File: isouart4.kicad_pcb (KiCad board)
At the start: 2 copper layers, 89 x 99 mm, 78 parts, among them J1 USB_B, J2 Conn_01x04, J3 Conn_01x04, J4 Conn_01x04, J5 Conn_01x04, U1 CH344Q, U10 74HC123, U11 74HC123, U12 74HC123, U13 74HC123, U2 π122U31, U3 AMS1117-3.3, U4 π122U31, U5 π122U31, U6 π122U31, X1 ASV-xxxMHz

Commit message: pcb-route all uart channels
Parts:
- removed C4: 100n, Capacitor_SMD:C_0805_2012Metric_Pad1.18x1.45mm_HandSolder
- removed C6: 12p, Capacitor_SMD:C_0805_2012Metric_Pad1.18x1.45mm_HandSolder
- removed L3: L_Ferrite_Small, Inductor_SMD:L_TDK_NLV25_2.5x2.0mm
- removed X1: ASV-xxxMHz, Oscillator:Oscillator_SMD_Abracon_ASV-4Pin_7.0x5.1mm
- added C10: 100n, Capacitor_SMD:C_0805_2012Metric_Pad1.18x1.45mm_HandSolder, B.Cu at (191.2, 127.7)
- added C32: 22p, Capacitor_SMD:C_0805_2012Metric_Pad1.18x1.45mm_HandSolder, B.Cu at (166.9, 100.9)
- added C33: 22p, Capacitor_SMD:C_0805_2012Metric_Pad1.18x1.45mm_HandSolder, B.Cu at (175.1, 100.0)
- added C8: 100n, Capacitor_SMD:C_0805_2012Metric_Pad1.18x1.45mm_HandSolder, B.Cu at (192.2, 65.2)
- added C9: 100n, Capacitor_SMD:C_0805_2012Metric_Pad1.18x1.45mm_HandSolder, B.Cu at (192.0, 106.9)
- added Y2: 8MHz, Crystal:Crystal_SMD_7050-4Pin_7.0x5.0mm, B.Cu at (170.6, 104.7)
- C22, C23, C24: moved to B.Cu
- C3: footprint Capacitor_SMD:C_0603_1608Metric_Pad1.08x0.95mm_HandSolder -> Capacitor_SMD:C_0805_2012Metric_Pad1.18x1.45mm_HandSolder; moved to B.Cu
- moved C16 17.7 mm to (209.8, 126.4), turned to -90 degrees
- moved C24 17.4 mm to (200.2, 128.7), turned to 90 degrees
- moved C15 15.1 mm to (209.6, 106.0), turned to -90 degrees
- moved R8 14.4 mm to (200.7, 73.4), turned to 180 degrees
- moved C20 14.2 mm to (204.8, 124.8), turned to 90 degrees
- moved C23 14.0 mm to (200.3, 108.3), turned to 90 degrees
- moved R5 12.6 mm to (215.8, 94.5)
- moved U13 12.1 mm to (207.2, 123.7), turned to 180 degrees
- moved R17 12.1 mm to (204.6, 99.9), turned to 180 degrees
- moved R6 11.6 mm to (215.5, 114.8)
- moved C19 11.3 mm to (204.4, 104.4), turned to 90 degrees
- moved R4 11.0 mm to (215.7, 73.4)
- moved U12 9.35 mm to (207.1, 103.4), turned to 180 degrees
- moved C18 9.31 mm to (204.8, 83.5), turned to 90 degrees
- moved R12 9.22 mm to (209.5, 80.5)
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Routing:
- net /indicators-ch2/V+MON: track 0.00 -> 55.9 mm, vias 0 -> 3
- net /indicators-ch3/V+MON: track 0.00 -> 55.5 mm, vias 0 -> 3
- net /indicators-ch4/V+MON: track 0.00 -> 53.3 mm, vias 0 -> 3
- net /indicators-ch4/RXMON: track 0.00 -> 30.4 mm, vias 0 -> 2
- net /indicators-ch2/TXMON: track 0.00 -> 29.7 mm, vias 0 -> 2
- net /indicators-ch4/TXMON: track 0.00 -> 29.7 mm, vias 0 -> 2
- net /indicators-ch3/TXMON: track 0.00 -> 29.7 mm, vias 0 -> 2
- net /indicators-ch3/RXMON: track 0.00 -> 29.2 mm, vias 0 -> 2
- net /indicators-ch2/RXMON: track 0.00 -> 29.1 mm, vias 0 -> 2
- net /indicators-ch1/GNDMON: track 29.1 -> 0.00 mm, vias 2 -> 10
- net /USB-UART4-CH344Q/XO: track 0.00 -> 13.8 mm
- net /indicators-ch1/V+MON: track 71.3 -> 57.8 mm, vias 4 -> 3
- net Net-(U13A-~{Q}): track 0.00 -> 12.9 mm, vias 0 -> 1
- net Net-(U11A-~{Q}): track 0.00 -> 12.9 mm, vias 0 -> 1
- net Net-(U12A-~{Q}): track 0.00 -> 12.9 mm, vias 0 -> 1
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- added copper zone on B.Cu, net /indicators-ch1/V+MON
- added copper zone on B.Cu, net /indicators-ch2/GNDMON
- added copper zone on F.Cu, net /indicators-ch2/GNDMON
- added copper zone on B.Cu, net /indicators-ch2/V+MON
- added copper zone on B.Cu, net /indicators-ch3/GNDMON
- added copper zone on F.Cu, net /indicators-ch3/GNDMON
- added copper zone on B.Cu, net /indicators-ch3/V+MON
- added copper zone on B.Cu, net /indicators-ch4/GNDMON
- added copper zone on F.Cu, net /indicators-ch4/GNDMON
- added copper zone on B.Cu, net /indicators-ch4/V+MON

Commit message: Flush latest changes
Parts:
- added C11: 4n7, Capacitor_SMD:C_0805_2012Metric_Pad1.18x1.45mm_HandSolder, B.Cu at (146.5, 120.3)
- added F1: 500mA, anotherfuse:FuseX, B.Cu at (150.7, 107.4)
- added R25: 4K7, Resistor_SMD:R_0805_2012Metric_Pad1.20x1.40mm_HandSolder, B.Cu at (146.4, 117.3)
- C21, C22, C23, C24: value 1uF -> 100n
- H1, H2, H3, H4: footprint MountingHole:MountingHole_3.2mm_M3 -> MountingHole:MountingHole_3.2mm_M3_Pad_Via
- R10, R19, R2, R20, R24, R3, R4, R5, R6, R7, R8, R9: moved to B.Cu
- moved L1 21.3 mm to (152.7, 85.8)
- moved C5 7.11 mm to (170.3, 80.9)
- moved L2 6.25 mm to (157.8, 121.3), turned to -90 degrees
- moved R5 2.47 mm to (213.3, 94.5)
- moved R6 2.26 mm to (213.2, 114.8)
- moved R4 2.23 mm to (213.5, 73.4)
- moved R7 1.31 mm to (200.6, 50.8), turned to 180 degrees
- moved R19 1.03 mm to (183.0, 80.4)
- moved R2 1.00 mm to (213.4, 50.8), turned to 0 degrees
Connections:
- L1 pad 1: Net-(J1-VBUS) -> Net-(F1-Pad2)
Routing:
- net Net-(U3-VI): track 55.5 -> 34.2 mm
- net Net-(F1-Pad2): track 0.00 -> 11.8 mm
- net /USB-UART4-CH344Q/VIN 3.3V: track 181.4 -> 174.0 mm, vias 22 -> 9
- net /GNDUSBCONN: track 18.8 -> 12.5 mm
- net /USBSHLD: track 10.5 -> 14.9 mm
- net Net-(J1-VBUS): track 8.42 -> 11.6 mm
- net Net-(D8-K2): track 5.23 -> 2.62 mm
- net Net-(U10A-~{Q}): track 11.2 -> 13.6 mm, vias 1 -> 0
- net Net-(D6-K2): track 5.26 -> 2.95 mm
- net Net-(D7-K2): track 5.26 -> 2.98 mm
- net /USB-UART4-CH344Q/ACT: track 56.2 -> 58.5 mm, vias 1 -> 2
- net Net-(U10B-~{Q}): track 12.1 -> 14.1 mm, vias 1 -> 0
- net Net-(D5-K1): track 4.77 -> 2.91 mm
- net Net-(U13A-~{Q}): track 12.9 -> 11.7 mm, vias 1 -> 0
- net Net-(U12A-~{Q}): track 12.9 -> 11.7 mm, vias 1 -> 0
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- added copper zone on B.Cu, net /SHLD
- added copper zone on F.Cu, net /SHLD

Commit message: remove problematic vias
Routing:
- net GND: vias 183 -> 181
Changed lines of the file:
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@@
   (via (at 164.725 104.525) (size 0.5) (drill 0.3) (layers "F.Cu" "B.Cu") (free) (net 1))
   (via (at 176.7 102.7) (size 0.5) (drill 0.3) (layers "F.Cu" "B.Cu") (free) (net 1))
-  (via (at 164.8 100.3) (size 0.5) (drill 0.3) (layers "F.Cu" "B.Cu") (free) (net 1))
   (via (at 166.5 98.4) (size 0.5) (drill 0.3) (layers "F.Cu" "B.Cu") (free) (net 1))
   (via (at 174.6 90.5) (size 0.5) (drill 0.3) (layers "F.Cu" "B.Cu") (free) (net 1))
@@
   (via (at 168.6 122.2) (size 0.5) (drill 0.3) (layers "F.Cu" "B.Cu") (net 1))
   (via (at 180.7 110.82) (size 0.5) (drill 0.3) (layers "F.Cu" "B.Cu") (free) (net 1))
-  (via (at 164.2 102) (size 0.5) (drill 0.3) (layers "F.Cu" "B.Cu") (free) (net 1))
   (via (at 165.4 103.6) (size 0.5) (drill 0.3) (layers "F.Cu" "B.Cu") (free) (net 1))
   (via (at 155.8 76.9) (size 0.5) (drill 0.3) (layers "F.Cu" "B.Cu") (free) (net 1))

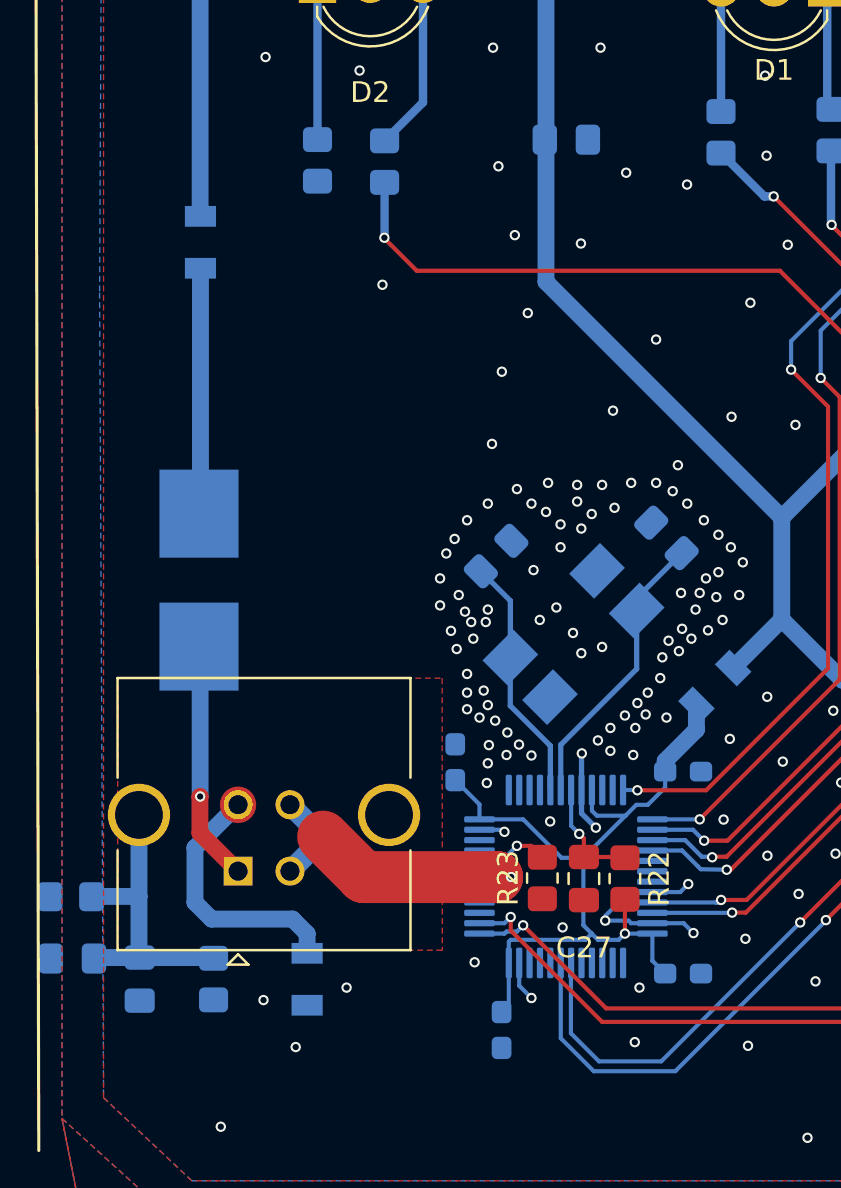
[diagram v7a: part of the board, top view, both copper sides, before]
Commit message: Restore 0805 capacitor footprints; Use anotherguse/FuseX copy form isouart4 lib
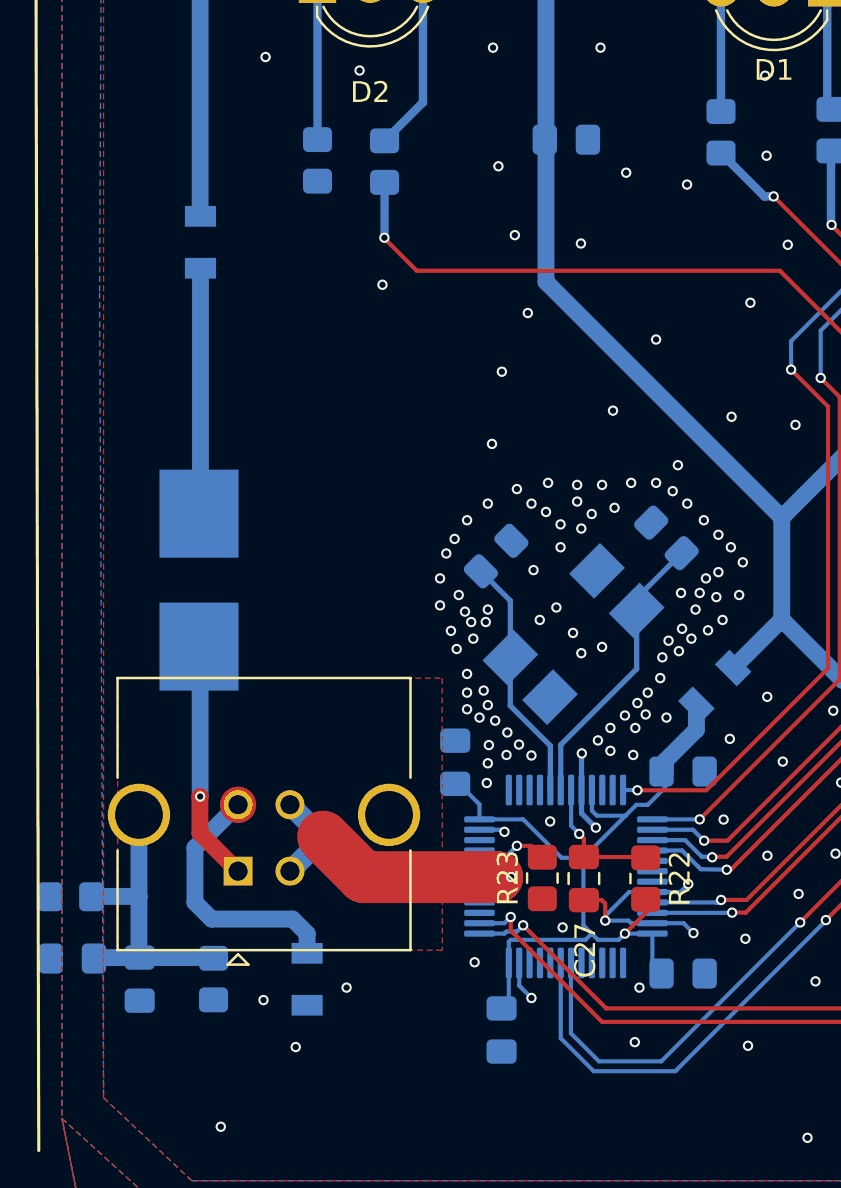
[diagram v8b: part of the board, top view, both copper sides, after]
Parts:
- C28, C29, C30, C31: footprint Capacitor_SMD:C_0603_1608Metric_Pad1.08x0.95mm_HandSolder -> Capacitor_SMD:C_0805_2012Metric_Pad1.18x1.45mm_HandSolder
- F1: footprint anotherfuse:FuseX -> isouart4:FuseX
- moved R22 1.00 mm to (174.1, 116.5)
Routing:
- net GND: track 33.2 -> 35.1 mm
- net /USB-UART4-CH344Q/RESET: track 5.54 -> 7.08 mm
- net Net-(C28-Pad2): track 39.3 -> 40.0 mm
